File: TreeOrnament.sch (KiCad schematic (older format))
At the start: 22 parts, among them J1 USB_B_Micro

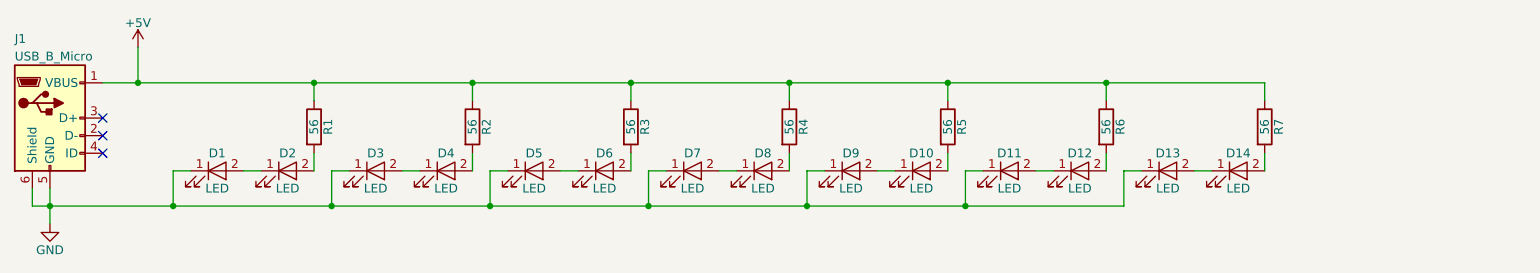
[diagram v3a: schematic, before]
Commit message: wire up LEDs in parallel
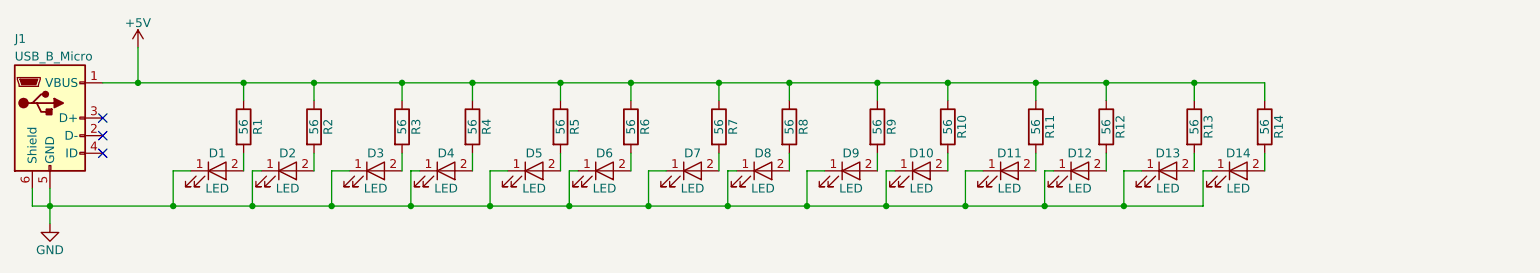
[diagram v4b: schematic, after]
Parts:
- added R1, R11, R13, R3, R5, R7, R9: 56, myLibrary:R_Axial_DIN0207_L6.3mm_D2.5mm_P7.62mm_Horizontal, symbol R
- renumbered R5 to R10, R6 to R12, R7 to R14, R1 to R2, R2 to R4, R3 to R6, R4 to R8
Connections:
- net +5V: now also R1.1, R11.1, R13.1, R3.1, R5.1, R7.1, R9.1
- net GND: now also D10.1 (K), D12.1 (K), D14.1 (K), D2.1 (K), D4.1 (K), D6.1 (K), D8.1 (K)
- net at D1.2 (A): now also R1.2; no longer D2.1 (K)
- net at D3.2 (A): now also R3.2; no longer D4.1 (K)
- net at D5.2 (A): now also R5.2; no longer D6.1 (K)
- net at D7.2 (A): now also R7.2; no longer D8.1 (K)
- net at D9.2 (A): now also R9.2; no longer D10.1 (K)
- net at D11.2 (A): now also R11.2; no longer D12.1 (K)
- net at D13.2 (A): now also R13.2; no longer D14.1 (K)
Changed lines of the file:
@@
 $EndComp
 $Comp
-L GND #PWR01
+L GND #PWR2
 U 1 1 59EFECD5
 P 1500 2000
-F 0 "#PWR01" H 1500 1750 50  0001 C CNN
+F 0 "#PWR2" H 1500 1750 50  0001 C CNN
 F 1 "GND" H 1500 1850 50  0000 C CNN
 F 2 "" H 1500 2000 50  0001 C CNN
@@
 $EndComp
 $Comp
-L +5V #PWR02
+L +5V #PWR1
 U 1 1 59EFED06
 P 2000 1000
-F 0 "#PWR02" H 2000 850 50  0001 C CNN
+F 0 "#PWR1" H 2000 850 50  0001 C CNN
 F 1 "+5V" H 2000 1140 50  0000 C CNN
 F 2 "" H 2000 1000 50  0001 C CNN
@@
 Connection ~ 1500 1900
 $Comp
-L R R1
+L R R2
 U 1 1 59EFED4B
 P 3000 1450
-F 0 "R1" V 3080 1450 50  0000 C CNN
+F 0 "R2" V 3080 1450 50  0000 C CNN
 F 1 "56" V 3000 1450 50  0000 C CNN
 F 2 "myLibrary:R_Axial_DIN0207_L6.3mm_D2.5mm_P7.62mm_Horizontal" V 2930 1450 50  0001 C CNN
@@
 	3000 1600 3000 1700
 Wire Wire Line
-	2700 1700 2600 1700
-Wire Wire Line
 	2300 1700 2200 1700
 Wire Wire Line
 	2200 1700 2200 1900
 $Comp
-L R R2
+L R R4
 U 1 1 59EFEE1B
 P 3900 1450
-F 0 "R2" V 3980 1450 50  0000 C CNN
+F 0 "R4" V 3980 1450 50  0000 C CNN
 F 1 "56" V 3900 1450 50  0000 C CNN
 F 2 "myLibrary:R_Axial_DIN0207_L6.3mm_D2.5mm_P7.62mm_Horizontal" V 3830 1450 50  0001 C CNN
@@
 	3900 1600 3900 1700
 Wire Wire Line
-	3600 1700 3500 1700
-Wire Wire Line
 	3200 1700 3100 1700
 Wire Wire Line
@@
 $EndComp
 $Comp
-L R R3
+L R R6
 U 1 1 59EFEF89
 P 4800 1450
-F 0 "R3" V 4880 1450 50  0000 C CNN
+F 0 "R6" V 4880 1450 50  0000 C CNN
 F 1 "56" V 4800 1450 50  0000 C CNN
 F 2 "myLibrary:R_Axial_DIN0207_L6.3mm_D2.5mm_P7.62mm_Horizontal" V 4730 1450 50  0001 C CNN
@@
 Wire Wire Line
 	4800 1600 4800 1700
-Wire Wire Line
-	4500 1700 4400 1700
 Wire Wire Line
 	4100 1700 4000 1700
@@
 $EndComp
 $Comp
-L R R4
+L R R8
 U 1 1 59EFF0C1
 P 5700 1450
-F 0 "R4" V 5780 1450 50  0000 C CNN
+F 0 "R8" V 5780 1450 50  0000 C CNN
 F 1 "56" V 5700 1450 50  0000 C CNN
 F 2 "myLibrary:R_Axial_DIN0207_L6.3mm_D2.5mm_P7.62mm_Horizontal" V 5630 1450 50  0001 C CNN
@@
 Wire Wire Line
 	5700 1600 5700 1700
-Wire Wire Line
-	5400 1700 5300 1700
 Wire Wire Line
 	5000 1700 4900 1700
@@
 $EndComp
 $Comp
-L R R5
+L R R10
 U 1 1 59F0ED78
 P 6600 1450
-F 0 "R5" V 6680 1450 50  0000 C CNN
+F 0 "R10" V 6680 1450 50  0000 C CNN
 F 1 "56" V 6600 1450 50  0000 C CNN
 F 2 "myLibrary:R_Axial_DIN0207_L6.3mm_D2.5mm_P7.62mm_Horizontal" V 6530 1450 50  0001 C CNN
@@
 Wire Wire Line
 	6600 1600 6600 1700
-Wire Wire Line
-	6300 1700 6200 1700
 Wire Wire Line
 	5900 1700 5800 1700
@@
 $EndComp
 $Comp
-L R R6
+L R R12
 U 1 1 59F0EF38
 P 7500 1450
-F 0 "R6" V 7580 1450 50  0000 C CNN
+F 0 "R12" V 7580 1450 50  0000 C CNN
 F 1 "56" V 7500 1450 50  0000 C CNN
 F 2 "myLibrary:R_Axial_DIN0207_L6.3mm_D2.5mm_P7.62mm_Horizontal" V 7430 1450 50  0001 C CNN
@@
 Wire Wire Line
 	7500 1600 7500 1700
-Wire Wire Line
-	7200 1700 7100 1700
 Wire Wire Line
 	6800 1700 6700 1700
@@
 $EndComp
 $Comp
-L R R7
+L R R14
 U 1 1 59F0F2FD
 P 8400 1450
-F 0 "R7" V 8480 1450 50  0000 C CNN
+F 0 "R14" V 8480 1450 50  0000 C CNN
 F 1 "56" V 8400 1450 50  0000 C CNN
 F 2 "myLibrary:R_Axial_DIN0207_L6.3mm_D2.5mm_P7.62mm_Horizontal" V 8330 1450 50  0001 C CNN
@@
 	8400 1600 8400 1700
 Wire Wire Line
-	8100 1700 8000 1700
-Wire Wire Line
 	7700 1700 7600 1700
 Wire Wire Line
@@
 Connection ~ 6700 1900
 Wire Wire Line
-	7600 1900 1400 1900
+	1400 1900 8050 1900
 Wire Wire Line
 	1800 1200 8400 1200
+$Comp
+L R R1
+U 1 1 59F4CC77
+P 2600 1450
+F 0 "R1" V 2680 1450 50  0000 C CNN
+F 1 "56" V 2600 1450 50  0000 C CNN
+F 2 "myLibrary:R_Axial_DIN0207_L6.3mm_D2.5mm_P7.62mm_Horizontal" V 2530 1450 50  0001 C CNN
+F 3 "" H 2600 1450 50  0001 C CNN
+	1    2600 1450
+	1    0    0    -1
+$EndComp
+$Comp
+L R R3
+U 1 1 59F4CCD0
+P 3500 1450
+F 0 "R3" V 3580 1450 50  0000 C CNN
+F 1 "56" V 3500 1450 50  0000 C CNN
+F 2 "myLibrary:R_Axial_DIN0207_L6.3mm_D2.5mm_P7.62mm_Horizontal" V 3430 1450 50  0001 C CNN
+F 3 "" H 3500 1450 50  0001 C CNN
+	1    3500 1450
+	1    0    0    -1
+$EndComp
+$Comp
+L R R5
+U 1 1 59F4CD2C
+P 4400 1450
+F 0 "R5" V 4480 1450 50  0000 C CNN
+F 1 "56" V 4400 1450 50  0000 C CNN
+F 2 "myLibrary:R_Axial_DIN0207_L6.3mm_D2.5mm_P7.62mm_Horizontal" V 4330 1450 50  0001 C CNN
+F 3 "" H 4400 1450 50  0001 C CNN
+	1    4400 1450
+	1    0    0    -1
+$EndComp
+$Comp
+L R R7
+U 1 1 59F4CD8B
+P 5300 1450
+F 0 "R7" V 5380 1450 50  0000 C CNN
+F 1 "56" V 5300 1450 50  0000 C CNN
+F 2 "myLibrary:R_Axial_DIN0207_L6.3mm_D2.5mm_P7.62mm_Horizontal" V 5230 1450 50  0001 C CNN
+F 3 "" H 5300 1450 50  0001 C CNN
+	1    5300 1450
+	1    0    0    -1
+$EndComp
+$Comp
+L R R9
+U 1 1 59F4CDEF
+P 6200 1450
+F 0 "R9" V 6280 1450 50  0000 C CNN
+F 1 "56" V 6200 1450 50  0000 C CNN
+F 2 "myLibrary:R_Axial_DIN0207_L6.3mm_D2.5mm_P7.62mm_Horizontal" V 6130 1450 50  0001 C CNN
+F 3 "" H 6200 1450 50  0001 C CNN
+	1    6200 1450
+	1    0    0    -1
+$EndComp
+$Comp
+L R R11
+U 1 1 59F4CE54
+P 7100 1450
+F 0 "R11" V 7180 1450 50  0000 C CNN
+F 1 "56" V 7100 1450 50  0000 C CNN
+F 2 "myLibrary:R_Axial_DIN0207_L6.3mm_D2.5mm_P7.62mm_Horizontal" V 7030 1450 50  0001 C CNN
+F 3 "" H 7100 1450 50  0001 C CNN
+	1    7100 1450
+	1    0    0    -1
+$EndComp
+$Comp
+L R R13
+U 1 1 59F4CEBC
+P 8000 1450
+F 0 "R13" V 8080 1450 50  0000 C CNN
+F 1 "56" V 8000 1450 50  0000 C CNN
+F 2 "myLibrary:R_Axial_DIN0207_L6.3mm_D2.5mm_P7.62mm_Horizontal" V 7930 1450 50  0001 C CNN
+F 3 "" H 8000 1450 50  0001 C CNN
+	1    8000 1450
+	1    0    0    -1
+$EndComp
+Wire Wire Line
+	2600 1300 2600 1200
+Connection ~ 2600 1200
+Wire Wire Line
+	2600 1600 2600 1700
+Wire Wire Line
+	3500 1200 3500 1300
+Connection ~ 3500 1200
+Wire Wire Line
+	3500 1600 3500 1700
+Wire Wire Line
+	2700 1700 2650 1700
+Wire Wire Line
+	2650 1700 2650 1900
+Connection ~ 2650 1900
+Wire Wire Line
+	3600 1700 3550 1700
+Wire Wire Line
+	3550 1700 3550 1900
+Connection ~ 3550 1900
+Wire Wire Line
+	4400 1200 4400 1300
+Connection ~ 4400 1200
+Wire Wire Line
+	4400 1600 4400 1700
+Wire Wire Line
+	4500 1700 4450 1700
+Wire Wire Line
+	4450 1700 4450 1900
+Connection ~ 4450 1900
+Wire Wire Line
+	5300 1200 5300 1300
+Connection ~ 5300 1200
+Wire Wire Line
+	5300 1600 5300 1700
+Wire Wire Line
+	5400 1700 5350 1700
+Wire Wire Line
+	5350 1700 5350 1900
+Connection ~ 5350 1900
+Wire Wire Line
+	6200 1200 6200 1300
+Connection ~ 6200 1200
+Wire Wire Line
+	6200 1600 6200 1700
+Wire Wire Line
+	6300 1700 6250 1700
+Wire Wire Line
+	6250 1700 6250 1900
+Connection ~ 6250 1900
+Wire Wire Line
+	7100 1200 7100 1300
+Connection ~ 7100 1200
+Wire Wire Line
+	7100 1600 7100 1700
+Wire Wire Line
+	7200 1700 7150 1700
+Wire Wire Line
+	7150 1700 7150 1900
+Connection ~ 7150 1900
+Wire Wire Line
+	8000 1200 8000 1300
+Connection ~ 8000 1200
+Wire Wire Line
+	8000 1600 8000 1700
+Wire Wire Line
+	8100 1700 8050 1700
+Wire Wire Line
+	8050 1700 8050 1900
+Connection ~ 7600 1900
 $EndSCHEMATC

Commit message: Use smaller resistor footprint, e. g. for Stackpole CF18JT150R.
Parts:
- R1, R10, R11, R12, R13, R14, R2, R3, R4, R5, R6, R7, R8, R9: footprint myLibrary:R_Axial_DIN0207_L6.3mm_D2.5mm_P7.62mm_Horizontal -> myLibrary:R_Axial_DIN0204_L3.6mm_D1.6mm_P5.08mm_Horizontal
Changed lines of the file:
@@
 $EndComp
 $Comp
-L GND #PWR2
+L GND #PWR01
 U 1 1 59EFECD5
 P 1500 2000
-F 0 "#PWR2" H 1500 1750 50  0001 C CNN
+F 0 "#PWR01" H 1500 1750 50  0001 C CNN
 F 1 "GND" H 1500 1850 50  0000 C CNN
 F 2 "" H 1500 2000 50  0001 C CNN
@@
 $EndComp
 $Comp
-L +5V #PWR1
+L +5V #PWR02
 U 1 1 59EFED06
 P 2000 1000
-F 0 "#PWR1" H 2000 850 50  0001 C CNN
+F 0 "#PWR02" H 2000 850 50  0001 C CNN
 F 1 "+5V" H 2000 1140 50  0000 C CNN
 F 2 "" H 2000 1000 50  0001 C CNN
@@
 F 0 "R2" V 3080 1450 50  0000 C CNN
 F 1 "56" V 3000 1450 50  0000 C CNN
-F 2 "myLibrary:R_Axial_DIN0207_L6.3mm_D2.5mm_P7.62mm_Horizontal" V 2930 1450 50  0001 C CNN
+F 2 "myLibrary:R_Axial_DIN0204_L3.6mm_D1.6mm_P5.08mm_Horizontal" V 2930 1450 50  0001 C CNN
 F 3 "" H 3000 1450 50  0001 C CNN
 	1    3000 1450
@@
 F 0 "R4" V 3980 1450 50  0000 C CNN
 F 1 "56" V 3900 1450 50  0000 C CNN
-F 2 "myLibrary:R_Axial_DIN0207_L6.3mm_D2.5mm_P7.62mm_Horizontal" V 3830 1450 50  0001 C CNN
+F 2 "myLibrary:R_Axial_DIN0204_L3.6mm_D1.6mm_P5.08mm_Horizontal" V 3830 1450 50  0001 C CNN
 F 3 "" H 3900 1450 50  0001 C CNN
 	1    3900 1450
@@
 F 0 "R6" V 4880 1450 50  0000 C CNN
 F 1 "56" V 4800 1450 50  0000 C CNN
-F 2 "myLibrary:R_Axial_DIN0207_L6.3mm_D2.5mm_P7.62mm_Horizontal" V 4730 1450 50  0001 C CNN
+F 2 "myLibrary:R_Axial_DIN0204_L3.6mm_D1.6mm_P5.08mm_Horizontal" V 4730 1450 50  0001 C CNN
 F 3 "" H 4800 1450 50  0001 C CNN
 	1    4800 1450
@@
 F 0 "R8" V 5780 1450 50  0000 C CNN
 F 1 "56" V 5700 1450 50  0000 C CNN
-F 2 "myLibrary:R_Axial_DIN0207_L6.3mm_D2.5mm_P7.62mm_Horizontal" V 5630 1450 50  0001 C CNN
+F 2 "myLibrary:R_Axial_DIN0204_L3.6mm_D1.6mm_P5.08mm_Horizontal" V 5630 1450 50  0001 C CNN
 F 3 "" H 5700 1450 50  0001 C CNN
 	1    5700 1450
@@
 F 0 "R10" V 6680 1450 50  0000 C CNN
 F 1 "56" V 6600 1450 50  0000 C CNN
-F 2 "myLibrary:R_Axial_DIN0207_L6.3mm_D2.5mm_P7.62mm_Horizontal" V 6530 1450 50  0001 C CNN
+F 2 "myLibrary:R_Axial_DIN0204_L3.6mm_D1.6mm_P5.08mm_Horizontal" V 6530 1450 50  0001 C CNN
 F 3 "" H 6600 1450 50  0001 C CNN
 	1    6600 1450
@@
 F 0 "R12" V 7580 1450 50  0000 C CNN
 F 1 "56" V 7500 1450 50  0000 C CNN
-F 2 "myLibrary:R_Axial_DIN0207_L6.3mm_D2.5mm_P7.62mm_Horizontal" V 7430 1450 50  0001 C CNN
+F 2 "myLibrary:R_Axial_DIN0204_L3.6mm_D1.6mm_P5.08mm_Horizontal" V 7430 1450 50  0001 C CNN
 F 3 "" H 7500 1450 50  0001 C CNN
 	1    7500 1450
@@
 F 0 "R14" V 8480 1450 50  0000 C CNN
 F 1 "56" V 8400 1450 50  0000 C CNN
-F 2 "myLibrary:R_Axial_DIN0207_L6.3mm_D2.5mm_P7.62mm_Horizontal" V 8330 1450 50  0001 C CNN
+F 2 "myLibrary:R_Axial_DIN0204_L3.6mm_D1.6mm_P5.08mm_Horizontal" V 8330 1450 50  0001 C CNN
 F 3 "" H 8400 1450 50  0001 C CNN
 	1    8400 1450
@@
 F 0 "R1" V 2680 1450 50  0000 C CNN
 F 1 "56" V 2600 1450 50  0000 C CNN
-F 2 "myLibrary:R_Axial_DIN0207_L6.3mm_D2.5mm_P7.62mm_Horizontal" V 2530 1450 50  0001 C CNN
+F 2 "myLibrary:R_Axial_DIN0204_L3.6mm_D1.6mm_P5.08mm_Horizontal" V 2530 1450 50  0001 C CNN
 F 3 "" H 2600 1450 50  0001 C CNN
 	1    2600 1450
@@
 F 0 "R3" V 3580 1450 50  0000 C CNN
 F 1 "56" V 3500 1450 50  0000 C CNN
-F 2 "myLibrary:R_Axial_DIN0207_L6.3mm_D2.5mm_P7.62mm_Horizontal" V 3430 1450 50  0001 C CNN
+F 2 "myLibrary:R_Axial_DIN0204_L3.6mm_D1.6mm_P5.08mm_Horizontal" V 3430 1450 50  0001 C CNN
 F 3 "" H 3500 1450 50  0001 C CNN
 	1    3500 1450
@@
 F 0 "R5" V 4480 1450 50  0000 C CNN
 F 1 "56" V 4400 1450 50  0000 C CNN
-F 2 "myLibrary:R_Axial_DIN0207_L6.3mm_D2.5mm_P7.62mm_Horizontal" V 4330 1450 50  0001 C CNN
+F 2 "myLibrary:R_Axial_DIN0204_L3.6mm_D1.6mm_P5.08mm_Horizontal" V 4330 1450 50  0001 C CNN
 F 3 "" H 4400 1450 50  0001 C CNN
 	1    4400 1450
@@
 F 0 "R7" V 5380 1450 50  0000 C CNN
 F 1 "56" V 5300 1450 50  0000 C CNN
-F 2 "myLibrary:R_Axial_DIN0207_L6.3mm_D2.5mm_P7.62mm_Horizontal" V 5230 1450 50  0001 C CNN
+F 2 "myLibrary:R_Axial_DIN0204_L3.6mm_D1.6mm_P5.08mm_Horizontal" V 5230 1450 50  0001 C CNN
 F 3 "" H 5300 1450 50  0001 C CNN
 	1    5300 1450
@@
 F 0 "R9" V 6280 1450 50  0000 C CNN
 F 1 "56" V 6200 1450 50  0000 C CNN
-F 2 "myLibrary:R_Axial_DIN0207_L6.3mm_D2.5mm_P7.62mm_Horizontal" V 6130 1450 50  0001 C CNN
+F 2 "myLibrary:R_Axial_DIN0204_L3.6mm_D1.6mm_P5.08mm_Horizontal" V 6130 1450 50  0001 C CNN
 F 3 "" H 6200 1450 50  0001 C CNN
 	1    6200 1450
@@
 F 0 "R11" V 7180 1450 50  0000 C CNN
 F 1 "56" V 7100 1450 50  0000 C CNN
-F 2 "myLibrary:R_Axial_DIN0207_L6.3mm_D2.5mm_P7.62mm_Horizontal" V 7030 1450 50  0001 C CNN
+F 2 "myLibrary:R_Axial_DIN0204_L3.6mm_D1.6mm_P5.08mm_Horizontal" V 7030 1450 50  0001 C CNN
 F 3 "" H 7100 1450 50  0001 C CNN
 	1    7100 1450
@@
 F 0 "R13" V 8080 1450 50  0000 C CNN
 F 1 "56" V 8000 1450 50  0000 C CNN
-F 2 "myLibrary:R_Axial_DIN0207_L6.3mm_D2.5mm_P7.62mm_Horizontal" V 7930 1450 50  0001 C CNN
+F 2 "myLibrary:R_Axial_DIN0204_L3.6mm_D1.6mm_P5.08mm_Horizontal" V 7930 1450 50  0001 C CNN
 F 3 "" H 8000 1450 50  0001 C CNN
 	1    8000 1450

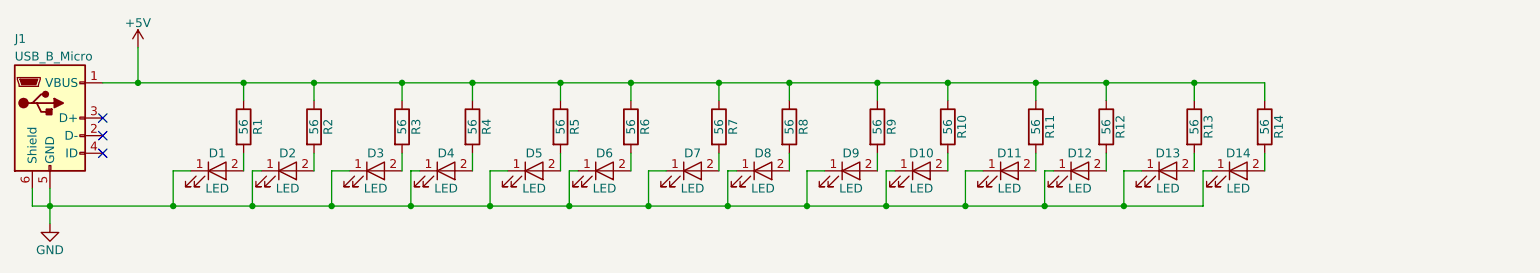
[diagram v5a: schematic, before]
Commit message: Use 150 Ohm resistors.
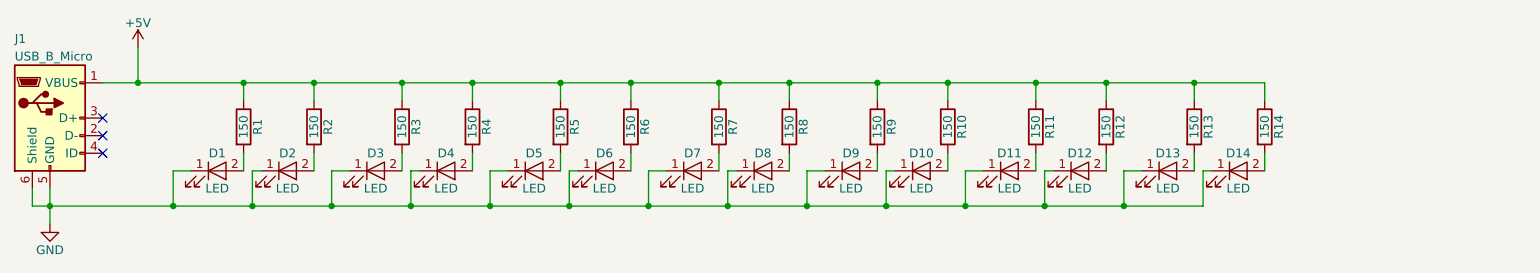
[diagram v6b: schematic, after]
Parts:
- R1, R10, R11, R12, R13, R14, R2, R3, R4, R5, R6, R7, R8, R9: value 56 -> 150
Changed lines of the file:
@@
 P 3000 1450
 F 0 "R2" V 3080 1450 50  0000 C CNN
-F 1 "56" V 3000 1450 50  0000 C CNN
+F 1 "150" V 3000 1450 50  0000 C CNN
 F 2 "myLibrary:R_Axial_DIN0204_L3.6mm_D1.6mm_P5.08mm_Horizontal" V 2930 1450 50  0001 C CNN
 F 3 "" H 3000 1450 50  0001 C CNN
@@
 P 3900 1450
 F 0 "R4" V 3980 1450 50  0000 C CNN
-F 1 "56" V 3900 1450 50  0000 C CNN
+F 1 "150" V 3900 1450 50  0000 C CNN
 F 2 "myLibrary:R_Axial_DIN0204_L3.6mm_D1.6mm_P5.08mm_Horizontal" V 3830 1450 50  0001 C CNN
 F 3 "" H 3900 1450 50  0001 C CNN
@@
 P 4800 1450
 F 0 "R6" V 4880 1450 50  0000 C CNN
-F 1 "56" V 4800 1450 50  0000 C CNN
+F 1 "150" V 4800 1450 50  0000 C CNN
 F 2 "myLibrary:R_Axial_DIN0204_L3.6mm_D1.6mm_P5.08mm_Horizontal" V 4730 1450 50  0001 C CNN
 F 3 "" H 4800 1450 50  0001 C CNN
@@
 P 5700 1450
 F 0 "R8" V 5780 1450 50  0000 C CNN
-F 1 "56" V 5700 1450 50  0000 C CNN
+F 1 "150" V 5700 1450 50  0000 C CNN
 F 2 "myLibrary:R_Axial_DIN0204_L3.6mm_D1.6mm_P5.08mm_Horizontal" V 5630 1450 50  0001 C CNN
 F 3 "" H 5700 1450 50  0001 C CNN
@@
 P 6600 1450
 F 0 "R10" V 6680 1450 50  0000 C CNN
-F 1 "56" V 6600 1450 50  0000 C CNN
+F 1 "150" V 6600 1450 50  0000 C CNN
 F 2 "myLibrary:R_Axial_DIN0204_L3.6mm_D1.6mm_P5.08mm_Horizontal" V 6530 1450 50  0001 C CNN
 F 3 "" H 6600 1450 50  0001 C CNN
@@
 P 7500 1450
 F 0 "R12" V 7580 1450 50  0000 C CNN
-F 1 "56" V 7500 1450 50  0000 C CNN
+F 1 "150" V 7500 1450 50  0000 C CNN
 F 2 "myLibrary:R_Axial_DIN0204_L3.6mm_D1.6mm_P5.08mm_Horizontal" V 7430 1450 50  0001 C CNN
 F 3 "" H 7500 1450 50  0001 C CNN
@@
 P 8400 1450
 F 0 "R14" V 8480 1450 50  0000 C CNN
-F 1 "56" V 8400 1450 50  0000 C CNN
+F 1 "150" V 8400 1450 50  0000 C CNN
 F 2 "myLibrary:R_Axial_DIN0204_L3.6mm_D1.6mm_P5.08mm_Horizontal" V 8330 1450 50  0001 C CNN
 F 3 "" H 8400 1450 50  0001 C CNN
@@
 P 2600 1450
 F 0 "R1" V 2680 1450 50  0000 C CNN
-F 1 "56" V 2600 1450 50  0000 C CNN
+F 1 "150" V 2600 1450 50  0000 C CNN
 F 2 "myLibrary:R_Axial_DIN0204_L3.6mm_D1.6mm_P5.08mm_Horizontal" V 2530 1450 50  0001 C CNN
 F 3 "" H 2600 1450 50  0001 C CNN
@@
 P 3500 1450
 F 0 "R3" V 3580 1450 50  0000 C CNN
-F 1 "56" V 3500 1450 50  0000 C CNN
+F 1 "150" V 3500 1450 50  0000 C CNN
 F 2 "myLibrary:R_Axial_DIN0204_L3.6mm_D1.6mm_P5.08mm_Horizontal" V 3430 1450 50  0001 C CNN
 F 3 "" H 3500 1450 50  0001 C CNN
@@
 P 4400 1450
 F 0 "R5" V 4480 1450 50  0000 C CNN
-F 1 "56" V 4400 1450 50  0000 C CNN
+F 1 "150" V 4400 1450 50  0000 C CNN
 F 2 "myLibrary:R_Axial_DIN0204_L3.6mm_D1.6mm_P5.08mm_Horizontal" V 4330 1450 50  0001 C CNN
 F 3 "" H 4400 1450 50  0001 C CNN
@@
 P 5300 1450
 F 0 "R7" V 5380 1450 50  0000 C CNN
-F 1 "56" V 5300 1450 50  0000 C CNN
+F 1 "150" V 5300 1450 50  0000 C CNN
 F 2 "myLibrary:R_Axial_DIN0204_L3.6mm_D1.6mm_P5.08mm_Horizontal" V 5230 1450 50  0001 C CNN
 F 3 "" H 5300 1450 50  0001 C CNN
@@
 P 6200 1450
 F 0 "R9" V 6280 1450 50  0000 C CNN
-F 1 "56" V 6200 1450 50  0000 C CNN
+F 1 "150" V 6200 1450 50  0000 C CNN
 F 2 "myLibrary:R_Axial_DIN0204_L3.6mm_D1.6mm_P5.08mm_Horizontal" V 6130 1450 50  0001 C CNN
 F 3 "" H 6200 1450 50  0001 C CNN
@@
 P 7100 1450
 F 0 "R11" V 7180 1450 50  0000 C CNN
-F 1 "56" V 7100 1450 50  0000 C CNN
+F 1 "150" V 7100 1450 50  0000 C CNN
 F 2 "myLibrary:R_Axial_DIN0204_L3.6mm_D1.6mm_P5.08mm_Horizontal" V 7030 1450 50  0001 C CNN
 F 3 "" H 7100 1450 50  0001 C CNN
@@
 P 8000 1450
 F 0 "R13" V 8080 1450 50  0000 C CNN
-F 1 "56" V 8000 1450 50  0000 C CNN
+F 1 "150" V 8000 1450 50  0000 C CNN
 F 2 "myLibrary:R_Axial_DIN0204_L3.6mm_D1.6mm_P5.08mm_Horizontal" V 7930 1450 50  0001 C CNN
 F 3 "" H 8000 1450 50  0001 C CNN

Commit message: Use newer version of Micro B footprint.
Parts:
- J1: footprint myLibrary:USB_Micro-B_Wuerth-614105150721_CircularHoles -> myLibrary:USB_Micro-B_Wuerth-614105150721_Vertical_CircularHoles
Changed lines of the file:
@@
 F 0 "J1" H 1300 1850 50  0000 L CNN
 F 1 "USB_B_Micro" H 1300 1750 50  0000 L CNN
-F 2 "myLibrary:USB_Micro-B_Wuerth-614105150721_CircularHoles" H 1650 1350 50  0001 C CNN
+F 2 "myLibrary:USB_Micro-B_Wuerth-614105150721_Vertical_CircularHoles" H 1650 1350 50  0001 C CNN
 F 3 "" H 1650 1350 50  0001 C CNN
 	1    1500 1400
